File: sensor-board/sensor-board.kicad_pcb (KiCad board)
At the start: 2 copper layers, 41.1 x 32 mm, 19 parts, among them J1 Conn_01x02, J2 Conn_01x03, J3 Conn_01x02, U1 NE5532

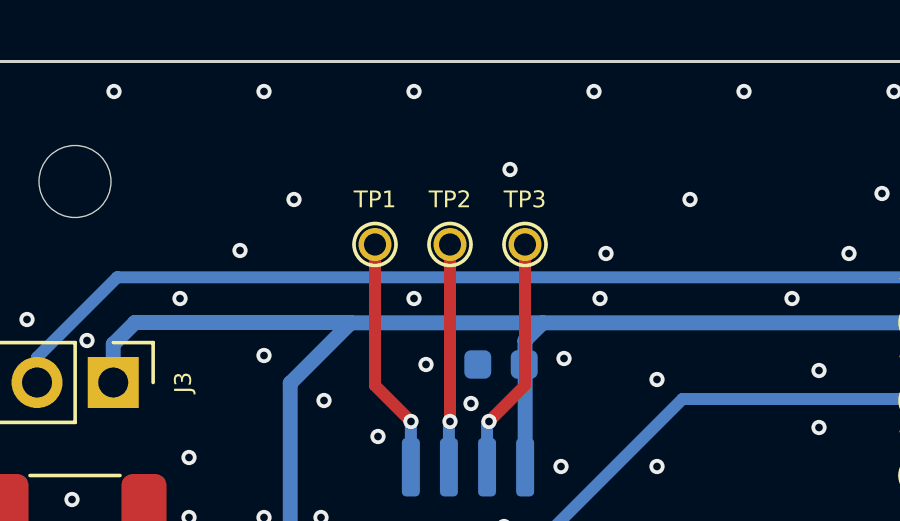
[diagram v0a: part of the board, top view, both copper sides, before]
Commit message: Added 0 ohms to U1B inputs
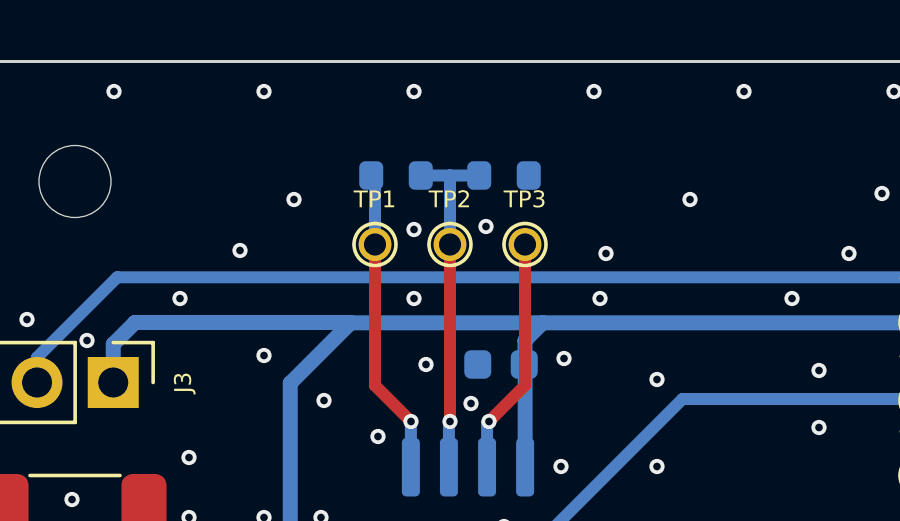
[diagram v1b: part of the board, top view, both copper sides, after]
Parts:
- added R4: 0, Resistor_SMD:R_0603_1608Metric, B.Cu at (118.4, 55.8)
- added R5: 0, Resistor_SMD:R_0603_1608Metric, B.Cu at (122.0, 55.8)
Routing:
- net Net-(U1B--): track 7.44 -> 11.7 mm
- net Net-(U1B-+): track 7.92 -> 10.3 mm
- net GND: vias 81 -> 82
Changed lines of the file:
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@@
+  )
+  (footprint "Resistor_SMD:R_0603_1608Metric" (layer "B.Cu")
+    (at 122 55.8 180)
+    (descr "Resistor SMD 0603 (1608 Metric), square (rectangular) end terminal, IPC_7351 nominal, (Body size source: IPC-SM-782 page 72, https://www.pcb-3d.com/wordpress/wp-content/uploads/ipc-sm-782a_amendment_1_and_2.pdf), generated with kicad-footprint-generator")
+    (tags "resistor")
+    (property "Sheetfile" "sensor-board.kicad_sch")
+    (property "Sheetname" "")
+    (property "ki_description" "Resistor, small US symbol")
+    (property "ki_keywords" "r resistor")
+    (attr smd)
+    (fp_text reference "R5" (at 0 1.43) (layer "B.SilkS")
+        (effects (font (size 1 1) (thickness 0.15)) (justify mirror))
+    )
+    (fp_text value "0" (at 0 -1.43) (layer "B.Fab")
+        (effects (font (size 1 1) (thickness 0.15)) (justify mirror))
+    )
+    (fp_text user "${REFERENCE}" (at 0 0) (layer "B.Fab")
+        (effects (font (size 0.4 0.4) (thickness 0.06)) (justify mirror))
+    )
+    (fp_line (start -0.237258 -0.5225) (end 0.237258 -0.5225)
+      (stroke (width 0.12) (type solid)) (layer "B.SilkS"))
+    (fp_line (start -0.237258 0.5225) (end 0.237258 0.5225)
+      (stroke (width 0.12) (type solid)) (layer "B.SilkS"))
+    (fp_line (start -1.48 -0.73) (end -1.48 0.73)
+      (stroke (width 0.05) (type solid)) (layer "B.CrtYd"))
+    (fp_line (start -1.48 0.73) (end 1.48 0.73)
+      (stroke (width 0.05) (type solid)) (layer "B.CrtYd"))
+    (fp_line (start 1.48 -0.73) (end -1.48 -0.73)
+      (stroke (width 0.05) (type solid)) (layer "B.CrtYd"))
+    (fp_line (start 1.48 0.73) (end 1.48 -0.73)
+      (stroke (width 0.05) (type solid)) (layer "B.CrtYd"))
+    (fp_line (start -0.8 -0.4125) (end -0.8 0.4125)
+      (stroke (width 0.1) (type solid)) (layer "B.Fab"))
+    (fp_line (start -0.8 0.4125) (end 0.8 0.4125)
+      (stroke (width 0.1) (type solid)) (layer "B.Fab"))
+    (fp_line (start 0.8 -0.4125) (end -0.8 -0.4125)
+      (stroke (width 0.1) (type solid)) (layer "B.Fab"))
+    (fp_line (start 0.8 0.4125) (end 0.8 -0.4125)
+      (stroke (width 0.1) (type solid)) (layer "B.Fab"))
+    (pad "1" smd roundrect (at -0.825 0 180) (size 0.8 0.95) (layers "B.Cu" "B.Paste" "B.Mask") (roundrect_rratio 0.25)
+      (net 3 "GND") (pintype "passive"))
+    (pad "2" smd roundrect (at 0.825 0 180) (size 0.8 0.95) (layers "B.Cu" "B.Paste" "B.Mask") (roundrect_rratio 0.25)
+      (net 8 "Net-(U1B--)") (pintype "passive"))
+    (model "${KICAD6_3DMODEL_DIR}/Resistor_SMD.3dshapes/R_0603_1608Metric.wrl"
+      (offset (xyz 0 0 0))
+      (scale (xyz 1 1 1))
+      (rotate (xyz 0 0 0))
+    )
   )
   (footprint "Resistor_SMD:R_0603_1608Metric" (layer "B.Cu")
@@
     (pad "2" smd roundrect (at 0.825 0) (size 0.8 0.95) (layers "B.Cu" "B.Paste" "B.Mask") (roundrect_rratio 0.25)
       (net 4 "Net-(J2-Pin_2)") (pintype "passive"))
+    (model "${KICAD6_3DMODEL_DIR}/Resistor_SMD.3dshapes/R_0603_1608Metric.wrl"
+      (offset (xyz 0 0 0))
+      (scale (xyz 1 1 1))
+      (rotate (xyz 0 0 0))
+    )
+  )
+  (footprint "Resistor_SMD:R_0603_1608Metric" (layer "B.Cu")
+    (at 118.4 55.8 180)
+    (descr "Resistor SMD 0603 (1608 Metric), square (rectangular) end terminal, IPC_7351 nominal, (Body size source: IPC-SM-782 page 72, https://www.pcb-3d.com/wordpress/wp-content/uploads/ipc-sm-782a_amendment_1_and_2.pdf), generated with kicad-footprint-generator")
+    (tags "resistor")
+    (property "Sheetfile" "sensor-board.kicad_sch")
+    (property "Sheetname" "")
+    (property "ki_description" "Resistor, small US symbol")
+    (property "ki_keywords" "r resistor")
+    (attr smd)
+    (fp_text reference "R4" (at 0 1.43) (layer "B.SilkS")
+        (effects (font (size 1 1) (thickness 0.15)) (justify mirror))
+    )
+    (fp_text value "0" (at 0 -1.43) (layer "B.Fab")
+        (effects (font (size 1 1) (thickness 0.15)) (justify mirror))
+    )
+    (fp_text user "${REFERENCE}" (at 0 0) (layer "B.Fab")
+        (effects (font (size 0.4 0.4) (thickness 0.06)) (justify mirror))
+    )
+    (fp_line (start -0.237258 -0.5225) (end 0.237258 -0.5225)
+      (stroke (width 0.12) (type solid)) (layer "B.SilkS"))
+    (fp_line (start -0.237258 0.5225) (end 0.237258 0.5225)
+      (stroke (width 0.12) (type solid)) (layer "B.SilkS"))
+    (fp_line (start -1.48 -0.73) (end -1.48 0.73)
+      (stroke (width 0.05) (type solid)) (layer "B.CrtYd"))
+    (fp_line (start -1.48 0.73) (end 1.48 0.73)
+      (stroke (width 0.05) (type solid)) (layer "B.CrtYd"))
+    (fp_line (start 1.48 -0.73) (end -1.48 -0.73)
+      (stroke (width 0.05) (type solid)) (layer "B.CrtYd"))
+    (fp_line (start 1.48 0.73) (end 1.48 -0.73)
+      (stroke (width 0.05) (type solid)) (layer "B.CrtYd"))
+    (fp_line (start -0.8 -0.4125) (end -0.8 0.4125)
+      (stroke (width 0.1) (type solid)) (layer "B.Fab"))
+    (fp_line (start -0.8 0.4125) (end 0.8 0.4125)
+      (stroke (width 0.1) (type solid)) (layer "B.Fab"))
+    (fp_line (start 0.8 -0.4125) (end -0.8 -0.4125)
+      (stroke (width 0.1) (type solid)) (layer "B.Fab"))
+    (fp_line (start 0.8 0.4125) (end 0.8 -0.4125)
+      (stroke (width 0.1) (type solid)) (layer "B.Fab"))
+    (pad "1" smd roundrect (at -0.825 0 180) (size 0.8 0.95) (layers "B.Cu" "B.Paste" "B.Mask") (roundrect_rratio 0.25)
+      (net 8 "Net-(U1B--)") (pintype "passive"))
+    (pad "2" smd roundrect (at 0.825 0 180) (size 0.8 0.95) (layers "B.Cu" "B.Paste" "B.Mask") (roundrect_rratio 0.25)
+      (net 7 "Net-(U1B-+)") (pintype "passive"))
     (model "${KICAD6_3DMODEL_DIR}/Resistor_SMD.3dshapes/R_0603_1608Metric.wrl"
       (offset (xyz 0 0 0))
@@
   (via (at 114 83) (size 0.508) (drill 0.254) (layers "F.Cu" "B.Cu") (free) (net 3))
   (via (at 125 83) (size 0.508) (drill 0.254) (layers "F.Cu" "B.Cu") (free) (net 3))
+  (via (at 119 57.6) (size 0.508) (drill 0.254) (layers "F.Cu" "B.Cu") (free) (net 3))
   (via (at 141.6 64.8) (size 0.508) (drill 0.254) (layers "F.Cu" "B.Cu") (free) (net 3))
   (via (at 114 53) (size 0.508) (drill 0.254) (layers "F.Cu" "B.Cu") (free) (net 3))
@@
   (via (at 131.6 59.9) (size 0.508) (drill 0.254) (layers "F.Cu" "B.Cu") (free) (net 3))
   (via (at 114 67.2) (size 0.508) (drill 0.254) (layers "F.Cu" "B.Cu") (free) (net 3))
-  (via (at 122.2 55.6) (size 0.508) (drill 0.254) (layers "F.Cu" "B.Cu") (free) (net 3))
+  (via (at 121.4 57.5) (size 0.508) (drill 0.254) (layers "F.Cu" "B.Cu") (free) (net 3))
   (via (at 141.6 59.8) (size 0.508) (drill 0.254) (layers "F.Cu" "B.Cu") (free) (net 3))
   (via (at 115.9 71.7) (size 0.508) (drill 0.254) (layers "F.Cu" "B.Cu") (free) (net 3))
@@
   (segment (start 118.9 64) (end 117.7 62.8) (width 0.4) (layer "F.Cu") (net 7))
   (via (at 118.9 64) (size 0.508) (drill 0.254) (layers "F.Cu" "B.Cu") (net 7))
+  (segment (start 117.7 55.925) (end 117.575 55.8) (width 0.4) (layer "B.Cu") (net 7))
+  (segment (start 117.7 58.1) (end 117.7 55.925) (width 0.4) (layer "B.Cu") (net 7))
   (segment (start 118.895 64.005) (end 118.9 64) (width 0.4) (layer "B.Cu") (net 7))
   (segment (start 118.895 65.525) (end 118.895 64.005) (width 0.4) (layer "B.Cu") (net 7))
   (segment (start 120.2 64) (end 120.2 58.1) (width 0.4) (layer "F.Cu") (net 8))
   (via (at 120.2 64) (size 0.508) (drill 0.254) (layers "F.Cu" "B.Cu") (net 8))
+  (segment (start 120.2 55.8) (end 121.175 55.8) (width 0.4) (layer "B.Cu") (net 8))
   (segment (start 120.165 64.035) (end 120.2 64) (width 0.4) (layer "B.Cu") (net 8))
+  (segment (start 120.2 55.8) (end 119.225 55.8) (width 0.4) (layer "B.Cu") (net 8))
   (segment (start 120.165 65.525) (end 120.165 64.035) (width 0.4) (layer "B.Cu") (net 8))
+  (segment (start 120.2 58.1) (end 120.2 55.8) (width 0.4) (layer "B.Cu") (net 8))
   (segment (start 121.5 64) (end 122.7 62.8) (width 0.4) (layer "F.Cu") (net 9))
   (segment (start 122.7 62.8) (end 122.7 58.1) (width 0.4) (layer "F.Cu") (net 9))
